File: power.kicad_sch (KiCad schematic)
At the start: 25 parts, among them J14 Molex_Nano-Fit_1x2_105309-1202, Q4 SI2337DS, U3 AP62301_TSOT

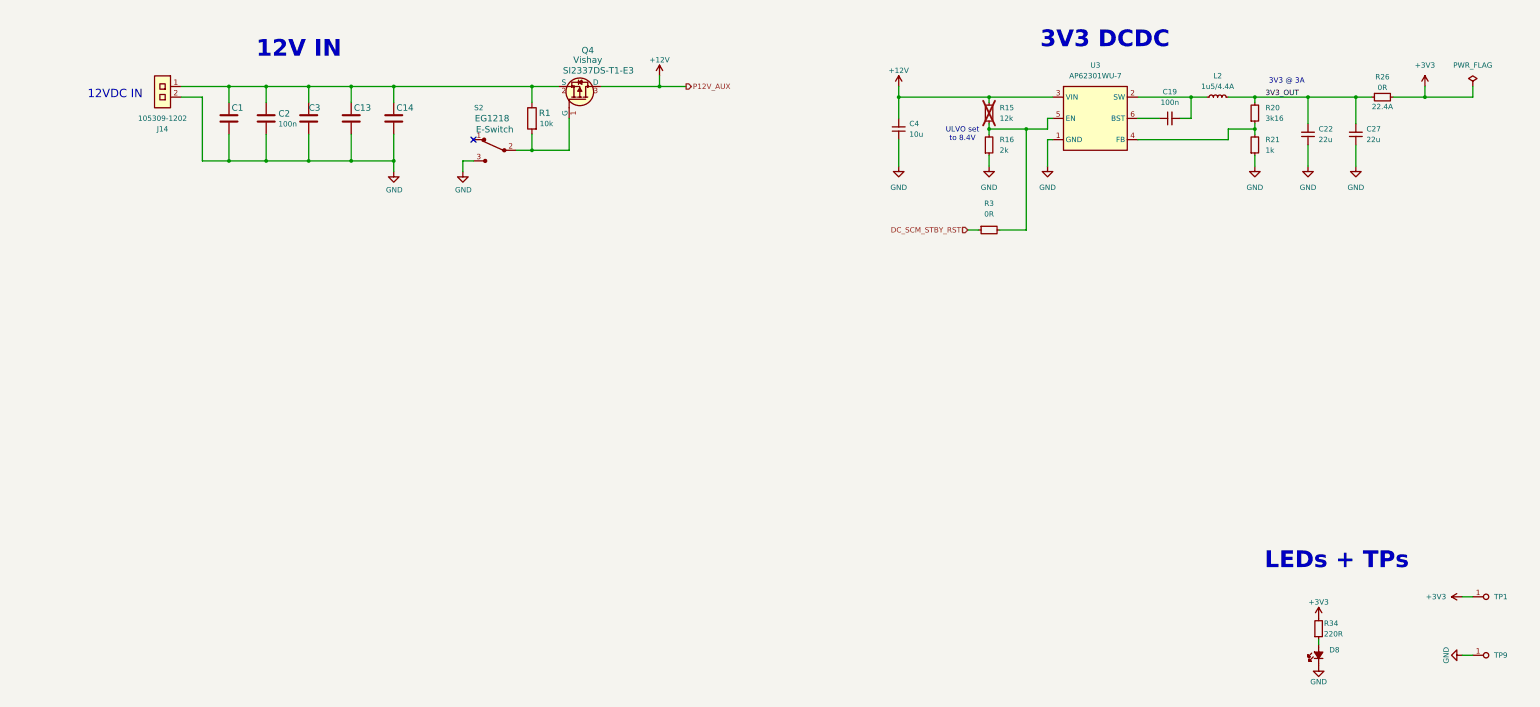
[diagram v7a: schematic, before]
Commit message: [#92504] Replace Power componenets with Antmicro library components
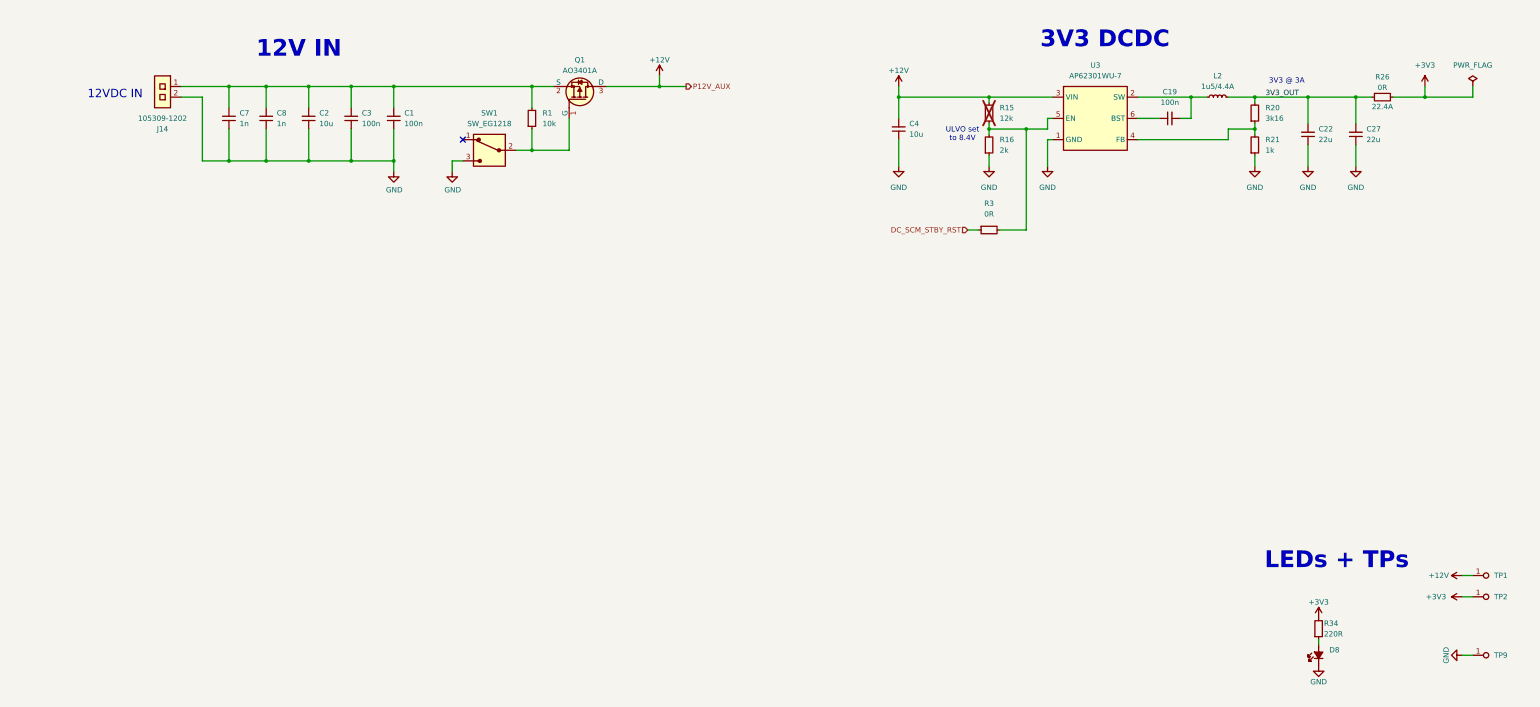
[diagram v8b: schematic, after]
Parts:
- removed C1, C14: C_1n_0603, bmc-breakout-board-footprints:0603-cap, symbol bmc-breakout-board:C_1n_0603
- removed C13, C2: C_100n_0402_16V, bmc-breakout-board-footprints:0402-cap, symbol bmc-breakout-board:C_100n_0402_16V
- removed C3: C_10u_25V_0603, bmc-breakout-board-footprints:0603-cap, symbol bmc-breakout-board:C_10u_25V_0603
- removed Q4: SI2337DS, bmc-breakout-board-footprints:SOT-23-3, symbol bmc-breakout-board:SI2337DS
- removed R1: R_10k_0402, bmc-breakout-board-footprints:0402-res, symbol bmc-breakout-board:R_10k_0402
- removed S2: EG1218, bmc-breakout-board-footprints:Switch_Slide_11.6x4mm_EG1218, symbol bmc-breakout-board:EG1218
- added C1, C3: C_100n_16V_X7R_0402, antmicro-footprints:C_0402_1005Metric, symbol antmicroCapacitors0402:C_100n_16V_X7R_0402
- added C2: C_10u_16V_0603, antmicro-footprints:C_0603_1608Metric, symbol antmicroCapacitors0603:C_10u_16V_0603
- added C7, C8: C_1n_16V_X7R_0402, antmicro-footprints:C_0402_1005Metric, symbol antmicroCapacitors0402:C_1n_16V_X7R_0402
- added Q1: AO3401A, antmicro-footprints:SOT-23-3, symbol antmicroTransistorsFETsMOSFETsSingle:AO3401A
- added R1: R_10k_0402, antmicro-footprints:R_0402_1005Metric, symbol antmicroResistors0402:R_10k_0402
- added SW1: SW_EG1218, antmicro-footprints:SW_Slide_E-Switch_EG1218, symbol antmicroSlideSwitches:SW_EG1218
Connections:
- net +12V: now also TP1.1, Q1.3 (D)
- net GND: now also C1.1, C2.1, C3.1, C7.1, C8.1, SW1.3
- net at J14.1: now also C1.2, C2.2, C3.2, C7.2, C8.2, Q1.2 (S), R1.2
- new net: Q1.1 (G), R1.1, SW1.2
